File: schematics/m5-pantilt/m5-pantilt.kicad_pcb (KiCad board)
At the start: 2 copper layers, 50 x 50 mm, 33 parts, among them J1 Conn_02x15_Odd_Even, J2 Conn_02x03_Odd_Even, J3 Conn_02x03_Odd_Even, J4 Conn_01x04, J5 BAT, J6 Conn_01x04, J7 5V_POWER, SW1 SW_SPDT, U1 TC7WH241FK

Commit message: Refine schematics
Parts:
- added Q1: IRLML6402, Package_TO_SOT_SMD:SOT-23, F.Cu at (132.8, 95.0)
- added R5: 1k, Resistor_SMD:R_0603_1608Metric_Pad1.05x0.95mm_HandSolder, F.Cu at (132.8, 92.2)
- D1: moved to F.Cu
- SW1: footprint Button_Switch_THT:SW_E-Switch_EG1224_SPDT_Angled -> Button_Switch_THT:SW_CuK_OS102011MA1QN1_SPDT_Angled; moved to B.Cu
- moved SW1 10.1 mm to (146.8, 61.0), turned to 270 degrees
- moved JP8 3.93 mm to (114.8, 83.9)
- moved JP5 3.93 mm to (114.8, 78.7)
- moved JP6 3.93 mm to (114.8, 81.3)
- moved JP7 3.93 mm to (114.8, 76.0)
- moved D1 3.84 mm to (125.4, 91.4), turned to 0 degrees
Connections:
- SW1 pad 1: Net-(SW1-Pad1) -> GND
- SW1 pad 2: Net-(J5-Pad1) -> Net-(Q1-Pad1)
- SW1 pad 3: Net-(D1-Pad2) -> Net-(SW1-Pad3)
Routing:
- net Net-(D1-Pad2): track 76.7 -> 31.5 mm, vias 0 -> 1
- net Net-(Q1-Pad1): track 0.00 -> 40.7 mm
- net Net-(J5-Pad1): track 38.0 -> 12.7 mm
- net /PWM2: track 22.9 -> 15.0 mm
- net /PWM1: track 15.9 -> 10.8 mm
- net /PWM1_C2: track 8.23 -> 5.87 mm
- net /PWM2_C1: track 14.7 -> 12.7 mm
- net /PWM1_C1: track 7.79 -> 5.81 mm
- net +5V: track 111.5 -> 109.5 mm
- net GND: vias 102 -> 93
- net (no net): vias 0 -> 3

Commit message: Refactor
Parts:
- moved SW1 1.00 mm to (145.8, 61.0)
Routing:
- net Net-(J2-Pad2): track 30.7 -> 18.9 mm, vias 1 -> 0
- net GND: track 6.71 -> 4.98 mm, vias 93 -> 95
- net Net-(D1-Pad2): track 31.5 -> 33.0 mm
- net Net-(Q1-Pad1): track 40.7 -> 41.7 mm
- net (no net): vias 3 -> 0

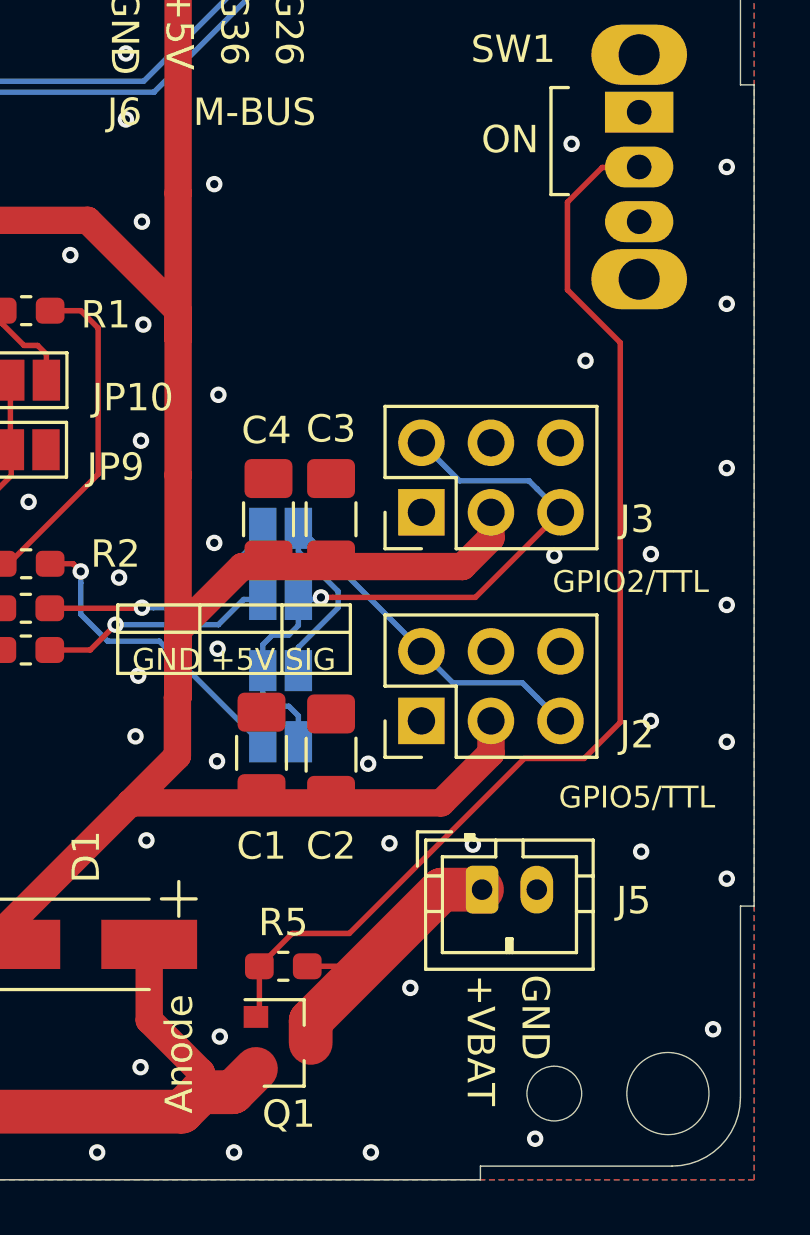
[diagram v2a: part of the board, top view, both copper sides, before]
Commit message: Fix MOSFET direction
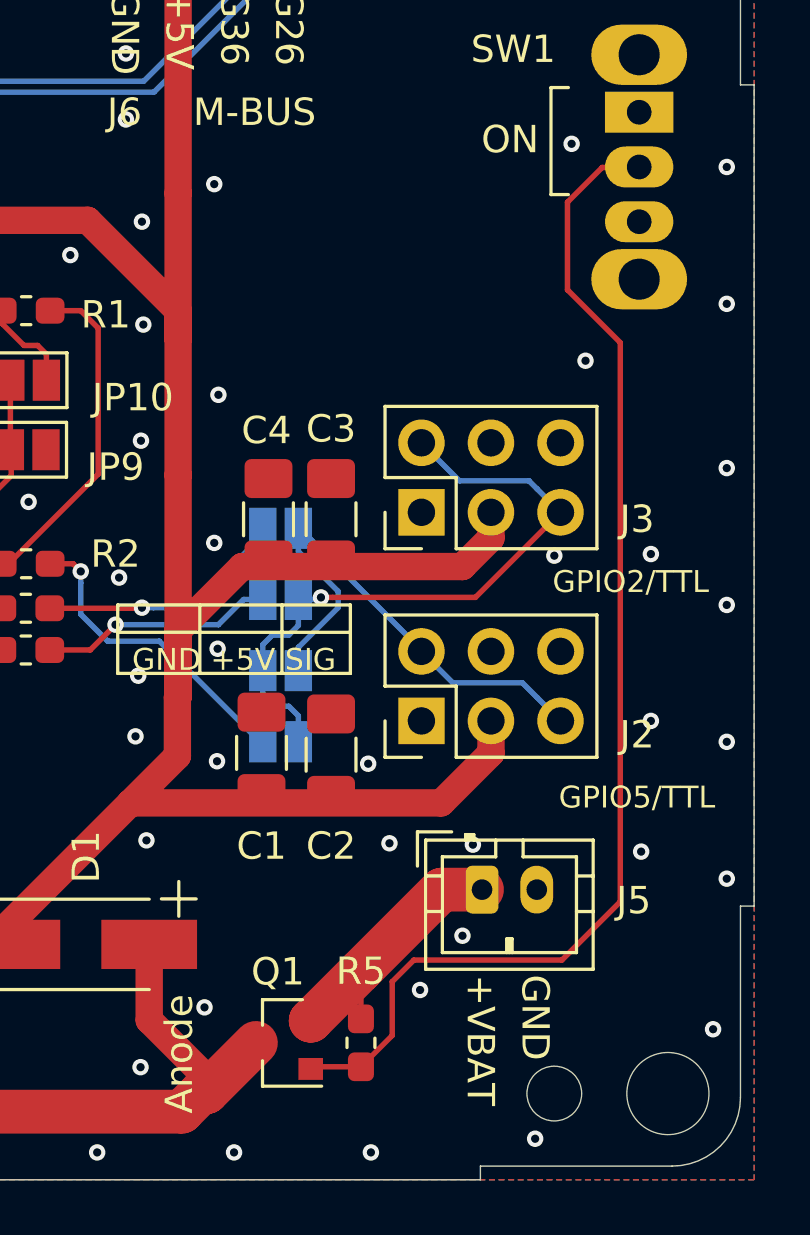
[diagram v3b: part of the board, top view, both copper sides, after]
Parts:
- moved R5 3.98 mm to (135.6, 95.0), turned to 90 degrees
- turned Q1 to 180 degrees
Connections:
- Q1 pad 2: Net-(D1-Pad2) -> Net-(J5-Pad1)
- Q1 pad 3: Net-(J5-Pad1) -> Net-(D1-Pad2)
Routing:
- net Net-(Q1-Pad1): track 41.7 -> 44.5 mm
- net Net-(J5-Pad1): track 13.2 -> 11.8 mm
- net GND: vias 95 -> 96
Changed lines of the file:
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@@
     (thickness 1.6)
     (drawings 73)
-    (tracks 342)
+    (tracks 345)
     (zones 0)
     (modules 35)
@@
     (34 B.Paste user)
     (35 F.Paste user)
-    (36 B.SilkS user)
+    (36 B.SilkS user hide)
     (37 F.SilkS user)
     (38 B.Mask user)
@@
   )
   (setup
-    (last_trace_width 0.2)
+    (last_trace_width 1)
     (user_trace_width 0.2)
     (user_trace_width 0.4)
@@
   )
   (module Package_TO_SOT_SMD:SOT-23 (layer F.Cu)
-    (at 132.8 95)
+    (at 132.8 95 180)
     (descr "SOT-23, Standard")
     (tags SOT-23)
@@
     (fp_line (start 0.76 -1.58) (end -1.4 -1.58) (layer F.SilkS) (width 0.12))
     (fp_line (start 0.76 1.58) (end -0.7 1.58) (layer F.SilkS) (width 0.12))
-    (pad 1 smd rect (at -1 -0.95) (size 0.9 0.8) (layers F.Cu F.Paste F.Mask)
+    (pad 1 smd rect (at -1 -0.95 180) (size 0.9 0.8) (layers F.Cu F.Paste F.Mask)
       (net 43 "Net-(Q1-Pad1)"))
-    (pad 2 smd rect (at -1 0.95) (size 0.9 0.8) (layers F.Cu F.Paste F.Mask)
+    (pad 2 smd rect (at -1 0.95 180) (size 0.9 0.8) (layers F.Cu F.Paste F.Mask)
+      (net 29 "Net-(J5-Pad1)"))
+    (pad 3 smd rect (at 1 0 180) (size 0.9 0.8) (layers F.Cu F.Paste F.Mask)
       (net 35 "Net-(D1-Pad2)"))
-    (pad 3 smd rect (at 1 0) (size 0.9 0.8) (layers F.Cu F.Paste F.Mask)
-      (net 29 "Net-(J5-Pad1)"))
     (model ${KISYS3DMOD}/Package_TO_SOT_SMD.3dshapes/SOT-23.wrl
       (at (xyz 0 0 0))
@@
   )
   (module Resistor_SMD:R_0603_1608Metric_Pad1.05x0.95mm_HandSolder (layer F.Cu)
-    (at 132.8 92.2)
+    (at 135.6362 94.9962 90)
     (descr "Resistor SMD 0603 (1608 Metric), square (rectangular) end terminal, IPC_7351 nominal with elongated pad for handsoldering. (Body size source: http://www.tortai-tech.com/upload/download/2011102023233369053.pdf), generated with kicad-footprint-generator")
     (tags "resistor handsolder")
     (attr smd)
-    (fp_text reference R5 (at 0 -1.6) (layer F.SilkS)
-      (effects (font (size 1 1) (thickness 0.15)))
-    )
-    (fp_text value 1k (at -3.2 -1.2) (layer F.Fab)
+    (fp_text reference R5 (at 2.6162 0 180) (layer F.SilkS)
+      (effects (font (size 1 1) (thickness 0.15)))
+    )
+    (fp_text value 1k (at -3.2 -1.2 90) (layer F.Fab)
       (effects (font (size 1 1) (thickness 0.15)))
     )
@@
     (fp_line (start 1.65 -0.73) (end 1.65 0.73) (layer F.CrtYd) (width 0.05))
     (fp_line (start 1.65 0.73) (end -1.65 0.73) (layer F.CrtYd) (width 0.05))
-    (fp_text user %R (at 0 0 270) (layer F.Fab)
+    (fp_text user %R (at 0 0 180) (layer F.Fab)
       (effects (font (size 0.4 0.4) (thickness 0.06)))
     )
-    (pad 1 smd roundrect (at -0.875 0) (size 1.05 0.95) (layers F.Cu F.Paste F.Mask) (roundrect_rratio 0.25)
+    (pad 1 smd roundrect (at -0.875 0 90) (size 1.05 0.95) (layers F.Cu F.Paste F.Mask) (roundrect_rratio 0.25)
       (net 43 "Net-(Q1-Pad1)"))
-    (pad 2 smd roundrect (at 0.875 0) (size 1.05 0.95) (layers F.Cu F.Paste F.Mask) (roundrect_rratio 0.25)
+    (pad 2 smd roundrect (at 0.875 0 90) (size 1.05 0.95) (layers F.Cu F.Paste F.Mask) (roundrect_rratio 0.25)
       (net 29 "Net-(J5-Pad1)"))
     (model ${KISYS3DMOD}/Resistor_SMD.3dshapes/R_0603_1608Metric.wrl
@@
   (via (at 127.6 73) (size 0.6) (drill 0.3) (layers F.Cu B.Cu) (net 1))
   (via (at 130.4292 71.3234) (size 0.6) (drill 0.3) (layers F.Cu B.Cu) (net 1))
-  (via (at 130.48 94.7676) (size 0.6) (drill 0.3) (layers F.Cu B.Cu) (net 1))
+  (via (at 129.9212 93.7008) (size 0.6) (drill 0.3) (layers F.Cu B.Cu) (net 1))
   (via (at 109 94.6) (size 0.6) (drill 0.3) (layers F.Cu B.Cu) (net 1))
   (via (at 143.3324 62.154) (size 0.6) (drill 0.3) (layers F.Cu B.Cu) (net 1))
@@
   (via (at 106.1976 82.3216) (size 0.6) (drill 0.3) (layers F.Cu B.Cu) (net 1))
   (via (at 139.7256 87.7572) (size 0.6) (drill 0.3) (layers F.Cu B.Cu) (net 1))
-  (via (at 137.4396 92.9896) (size 0.6) (drill 0.3) (layers F.Cu B.Cu) (net 1))
+  (via (at 137.7952 93.0658) (size 0.6) (drill 0.3) (layers F.Cu B.Cu) (net 1))
+  (via (at 139.3446 91.0846) (size 0.6) (drill 0.3) (layers F.Cu B.Cu) (net 1))
   (segment (start 128.956 54.9844) (end 129 54.9404) (width 1) (layer F.Cu) (net 2))
   (segment (start 128.956 63.9574) (end 128.956 54.9844) (width 1) (layer F.Cu) (net 2))
@@
   (segment (start 133.4 76.2) (end 137.846 80.646) (width 0.2) (layer B.Cu) (net 24))
   (segment (start 139.997199 89.337199) (end 140.06 89.4) (width 1.2) (layer F.Cu) (net 29))
-  (segment (start 136 92.2) (end 133.675 92.2) (width 0.2) (layer F.Cu) (net 29))
   (segment (start 137.2 91) (end 136 92.2) (width 0.2) (layer F.Cu) (net 29))
-  (segment (start 140.06 89.4) (end 138.5908 89.4) (width 1.6) (layer F.Cu) (net 29))
-  (segment (start 138.5908 89.4) (end 133.8 94.1908) (width 1.6) (layer F.Cu) (net 29))
-  (segment (start 133.8 94.1908) (end 133.8 95) (width 1.6) (layer F.Cu) (net 29))
+  (segment (start 133.8 94.185548) (end 133.8 94.1908) (width 1.6) (layer F.Cu) (net 29))
+  (segment (start 140.06 89.4) (end 138.585548 89.4) (width 1.6) (layer F.Cu) (net 29))
+  (segment (start 135.6362 92.3546) (end 135.6362 94.1212) (width 0.2) (layer F.Cu) (net 29))
+  (segment (start 138.585548 89.4) (end 135.633574 92.351974) (width 1.6) (layer F.Cu) (net 29))
+  (segment (start 135.633574 92.351974) (end 135.6362 92.3546) (width 0.2) (layer F.Cu) (net 29))
+  (segment (start 135.633574 92.351974) (end 133.8 94.185548) (width 1.6) (layer F.Cu) (net 29))
   (segment (start 120.05975 76.9782) (end 120.05975 77.478201) (width 0.2) (layer F.Cu) (net 30))
   (segment (start 124.281 68.25) (end 125.4 68.25) (width 0.2) (layer F.Cu) (net 30))
@@
   (segment (start 110.6 93.925998) (end 110.6 93.925998) (width 1.6) (layer B.Cu) (net 35))
   (via (at 110.6 93.925998) (size 0.6) (drill 0.3) (layers F.Cu B.Cu) (net 35))
-  (segment (start 130.95 96.8) (end 131.8 95.95) (width 1.6) (layer F.Cu) (net 35))
-  (segment (start 129.8 96.8) (end 130.95 96.8) (width 1.6) (layer F.Cu) (net 35))
   (segment (start 129.8 96.0688) (end 127.9 94.1688) (width 1) (layer F.Cu) (net 35))
   (segment (start 127.9 94.1688) (end 127.9 91.4) (width 1) (layer F.Cu) (net 35))
@@
   (segment (start 110.6 95.8172) (end 112.2936 97.5108) (width 1.6) (layer F.Cu) (net 35))
   (segment (start 110.6 93.925998) (end 110.6 95.8172) (width 1.6) (layer F.Cu) (net 35))
+  (segment (start 130 96.8) (end 131.8 95) (width 1.6) (layer F.Cu) (net 35))
+  (segment (start 129.8 96.8) (end 130 96.8) (width 1.6) (layer F.Cu) (net 35))
   (segment (start 132.05 76.45) (end 129.400004 79.099996) (width 0.2) (layer B.Cu) (net 36))
   (segment (start 129.400004 79.099996) (end 128.059464 79.099996) (width 0.2) (layer B.Cu) (net 36))
@@
   (segment (start 120.05975 76.4782) (end 120.6598 76.4782) (width 0.2) (layer F.Cu) (net 42))
   (segment (start 122.86 74.278) (end 122.86 72.695) (width 0.2) (layer F.Cu) (net 42))
-  (segment (start 131.8 94.05) (end 131.925 93.925) (width 0.2) (layer F.Cu) (net 43))
-  (segment (start 131.925 93.925) (end 131.925 92.2) (width 0.2) (layer F.Cu) (net 43))
-  (segment (start 144.45 63.0176) (end 145.7824 63.0176) (width 0.2) (layer F.Cu) (net 43))
-  (segment (start 145.7824 63.0176) (end 145.8 63) (width 0.2) (layer F.Cu) (net 43))
-  (segment (start 143.18 64.2876) (end 144.45 63.0176) (width 0.2) (layer F.Cu) (net 43))
-  (segment (start 143.18 67.488) (end 143.18 64.2876) (width 0.2) (layer F.Cu) (net 43))
-  (segment (start 145.1104 69.4184) (end 143.18 67.488) (width 0.2) (layer F.Cu) (net 43))
-  (segment (start 145.1104 83.2896) (end 145.1104 69.4184) (width 0.2) (layer F.Cu) (net 43))
-  (segment (start 143.7924 84.6076) (end 145.1104 83.2896) (width 0.2) (layer F.Cu) (net 43))
-  (segment (start 141.6052 84.6076) (end 143.7924 84.6076) (width 0.2) (layer F.Cu) (net 43))
-  (segment (start 135.2128 91) (end 141.6052 84.6076) (width 0.2) (layer F.Cu) (net 43))
-  (segment (start 133.125 91) (end 135.2128 91) (width 0.2) (layer F.Cu) (net 43))
-  (segment (start 131.925 92.2) (end 133.125 91) (width 0.2) (layer F.Cu) (net 43))
+  (segment (start 133.8788 95.8712) (end 133.8 95.95) (width 0.2) (layer F.Cu) (net 43))
+  (segment (start 135.6362 95.8712) (end 133.8788 95.8712) (width 0.2) (layer F.Cu) (net 43))
+  (segment (start 137.567596 91.9736) (end 136.7792 92.761996) (width 0.2) (layer F.Cu) (net 43))
+  (segment (start 142.9768 91.9736) (end 137.567596 91.9736) (width 0.2) (layer F.Cu) (net 43))
+  (segment (start 136.7792 94.7282) (end 135.6362 95.8712) (width 0.2) (layer F.Cu) (net 43))
+  (segment (start 136.7792 92.761996) (end 136.7792 94.7282) (width 0.2) (layer F.Cu) (net 43))
+  (segment (start 145.1104 89.84) (end 142.9768 91.9736) (width 0.2) (layer F.Cu) (net 43))
+  (segment (start 143.18 67.488) (end 145.1104 69.4184) (width 0.2) (layer F.Cu) (net 43))
+  (segment (start 143.18 64.2876) (end 143.18 67.488) (width 0.2) (layer F.Cu) (net 43))
+  (segment (start 144.45 63.0176) (end 143.18 64.2876) (width 0.2) (layer F.Cu) (net 43))
+  (segment (start 145.7824 63.0176) (end 144.45 63.0176) (width 0.2) (layer F.Cu) (net 43))
+  (segment (start 145.1104 69.4184) (end 145.1104 89.84) (width 0.2) (layer F.Cu) (net 43))
+  (segment (start 145.8 63) (end 145.7824 63.0176) (width 0.2) (layer F.Cu) (net 43))
   (zone (net 1) (net_name GND) (layer F.Cu) (hatch edge 0.508)
     (connect_pads (clearance 0.35))

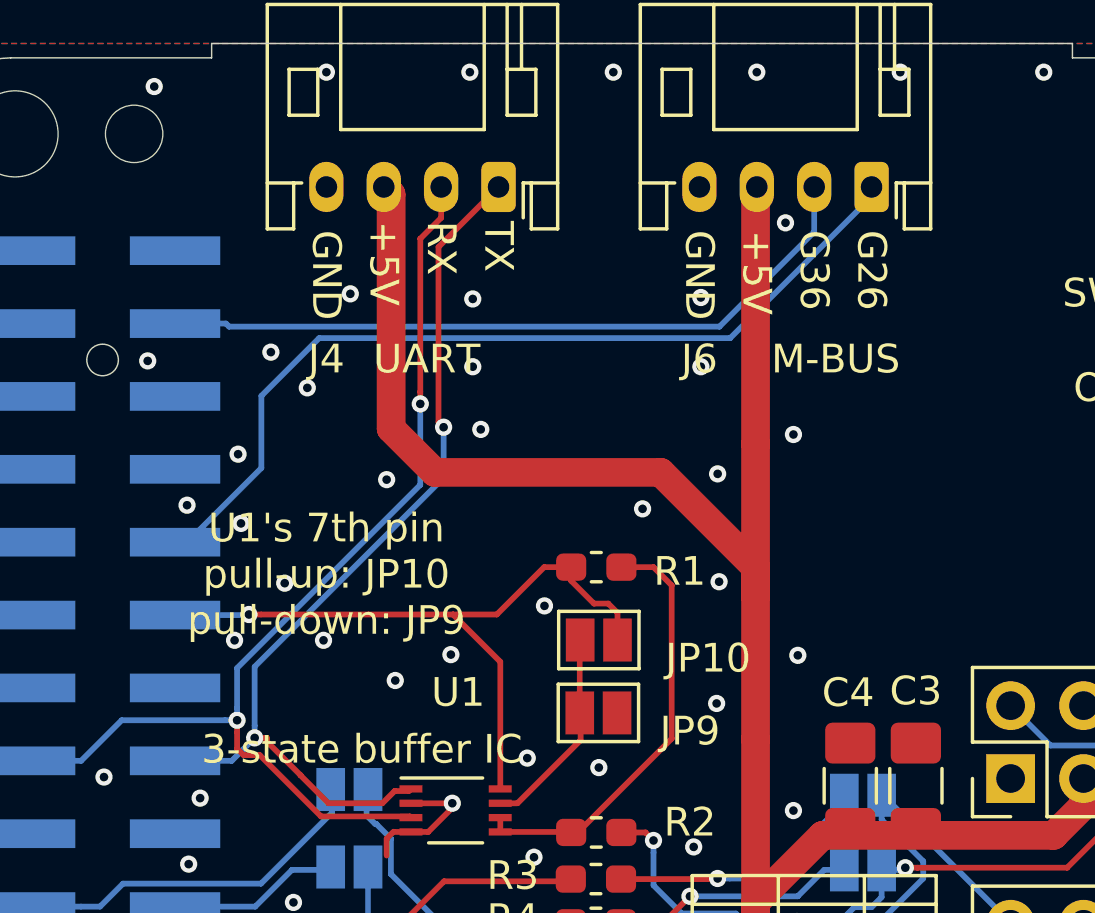
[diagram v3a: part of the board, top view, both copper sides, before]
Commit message: Fix #61 port bc assign (#62)
* Fix pin assign

* Fix silk

* Regenerate gerber
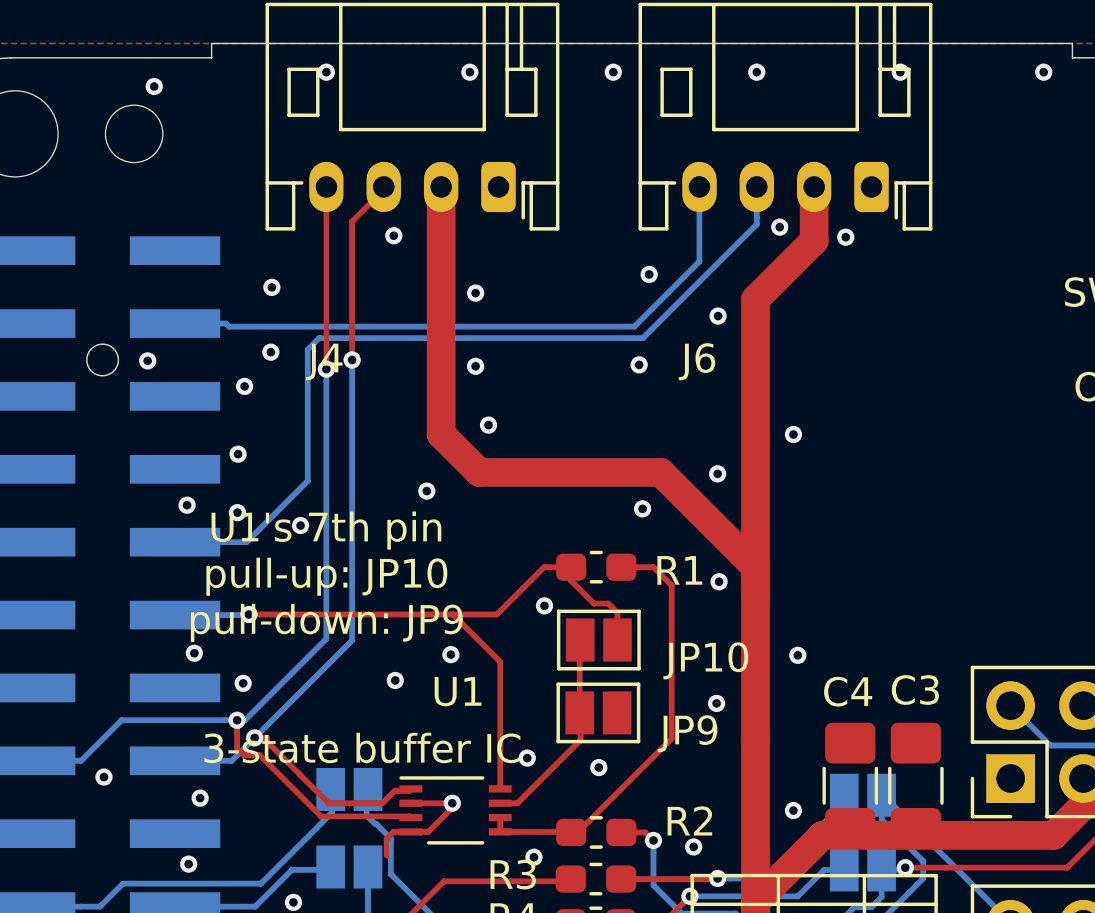
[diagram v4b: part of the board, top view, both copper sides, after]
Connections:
- J4 pad 1: /TXD2 -> GND
- J4 pad 2: /RXD2 -> +5V
- J4 pad 3: +5V -> /TXD2
- J4 pad 4: GND -> /RXD2
- J6 pad 1: /PORTB1 -> GND
- J6 pad 2: /PORTB2 -> +5V
- J6 pad 3: +5V -> /PORTB1
- J6 pad 4: GND -> /PORTB2
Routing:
- net /PORTB2: track 25.3 -> 21.9 mm
- net /PORTB1: track 31.1 -> 28.9 mm
- net /TXD2: track 32.7 -> 30.8 mm
- net /RXD2: track 37.4 -> 35.9 mm
- net +5V: track 109.5 -> 108.6 mm
- net GND: vias 96 -> 99
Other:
- board text added: "GPIO"
- board text removed: "M-BUS"

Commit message: Mark v0.2.1
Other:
- board text added: "m5-pantilt board v0.2.1 @meganetaaan"
- board text removed: "m5-pantilt board v0.2.0 @meganetaaan"
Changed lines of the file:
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@@
     (35 F.Paste user)
     (36 B.SilkS user)
-    (37 F.SilkS user hide)
+    (37 F.SilkS user)
     (38 B.Mask user)
     (39 F.Mask user)
@@
     (effects (font (size 1 1) (thickness 0.125)) (justify mirror))
   )
-  (gr_text "m5-pantilt board v0.2.0\n@meganetaaan" (at 133.7 95.2) (layer B.SilkS)
+  (gr_text "m5-pantilt board v0.2.1\n@meganetaaan" (at 133.7 95.2) (layer B.SilkS)
     (effects (font (size 1.2 1.2) (thickness 0.3)) (justify mirror))
   )

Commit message: WIP: fix schematics
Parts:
- removed D1: D, Diode_SMD:D_SMA_Handsoldering
- removed JP1, JP2, JP3, JP4, JP5, JP6, JP7, JP8: Jumper_2_Open, Jumper:SolderJumper-2_P1.3mm_Open_Pad1.0x1.5mm
- added R10: 0, Resistor_SMD:R_0603_1608Metric_Pad1.05x0.95mm_HandSolder, F.Cu at (69.2, 69.0)
- added R11: 0, Resistor_SMD:R_0603_1608Metric_Pad1.05x0.95mm_HandSolder, F.Cu at (73.5, 66.5)
- added R12: 0, Resistor_SMD:R_0603_1608Metric_Pad1.05x0.95mm_HandSolder, F.Cu at (69.2, 71.5)
- added R13: 0, Resistor_SMD:R_0603_1608Metric_Pad1.05x0.95mm_HandSolder, F.Cu at (73.5, 69.0)
- added R14: 0, Resistor_SMD:R_0603_1608Metric_Pad1.05x0.95mm_HandSolder, F.Cu at (133.0, 68.2)
- added R15: 0, Resistor_SMD:R_0603_1608Metric_Pad1.05x0.95mm_HandSolder, F.Cu at (73.5, 71.5)
- added R16: 0, Resistor_SMD:R_0603_1608Metric_Pad1.05x0.95mm_HandSolder, F.Cu at (77.9, 69.0)
- added R6: 10k, Resistor_SMD:R_0603_1608Metric_Pad1.05x0.95mm_HandSolder, F.Cu at (64.8, 66.5)
- added R7: 0, Resistor_SMD:R_0603_1608Metric_Pad1.05x0.95mm_HandSolder, F.Cu at (64.8, 69.0)
- added R8: 0, Resistor_SMD:R_0603_1608Metric_Pad1.05x0.95mm_HandSolder, F.Cu at (69.2, 66.5)
- added R9: 0, Resistor_SMD:R_0603_1608Metric_Pad1.05x0.95mm_HandSolder, F.Cu at (64.8, 71.5)
- R5: value 1k -> 47k
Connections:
- U1 pad 7: Net-(JP10-Pad2) -> Net-(R15-Pad1)
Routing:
- net Net-(J3-Pad2): track 24.5 -> 6.47 mm, vias 1 -> 0
- net Net-(R14-Pad1): track 11.4 -> 0.00 mm, vias 1 -> 0
- net Net-(J1-Pad29): track 33.3 -> 27.2 mm
